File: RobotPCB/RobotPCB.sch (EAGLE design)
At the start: 42 parts, among them IC1 MPU6050, IC2 MCP73831/OT, U1 DRV8835, U2 CP2104-F03-GM

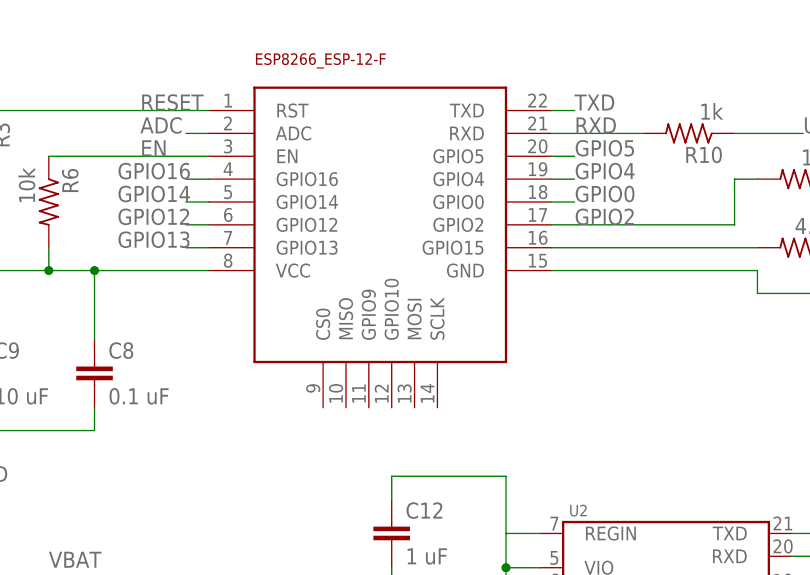
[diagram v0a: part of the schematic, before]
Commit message: Added text to pins
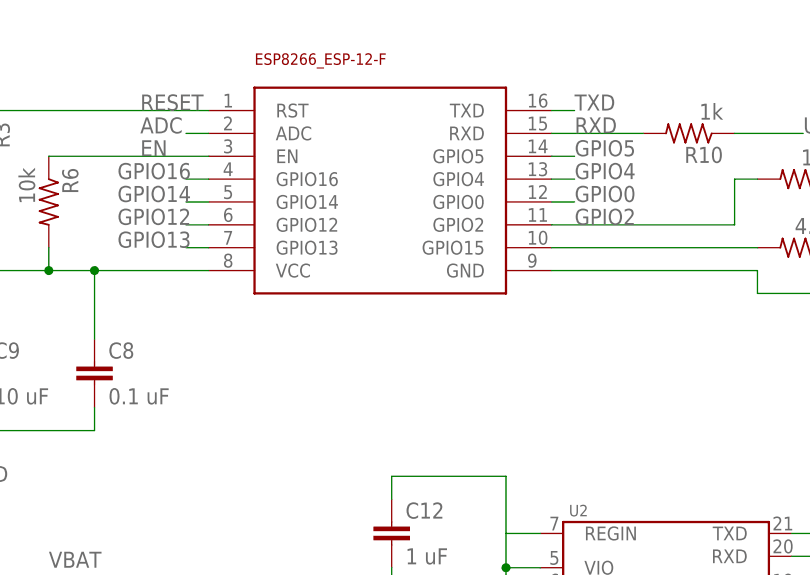
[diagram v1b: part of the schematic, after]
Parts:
- U$1: device ESP8266-ESP12:ESP8266_ESP-12 -> ESP8266:ESP8266_ESP-12
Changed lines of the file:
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@@
 <part name="JP1" library="pinhead" library_urn="urn:adsk.eagle:library:325" deviceset="PINHD-1X8" device="" package3d_urn="urn:adsk.eagle:package:22409/2"/>
 <part name="JP2" library="pinhead" library_urn="urn:adsk.eagle:library:325" deviceset="PINHD-1X8" device="" package3d_urn="urn:adsk.eagle:package:22409/2"/>
-<part name="U$1" library="ESP8266-ESP12" deviceset="ESP8266_ESP-12" device=""/>
+<part name="U$1" library="ESP8266" deviceset="ESP8266_ESP-12" device=""/>
 <part name="U2" library="silicon_labs" deviceset="CP2104" device="-F03-GM"/>
 <part name="Q1" library="semicon-smd-ipc" library_urn="urn:adsk.eagle:library:353" deviceset="NPN-TRANSISTOR_" device="SOT23" package3d_urn="urn:adsk.eagle:package:26310/1"/>
